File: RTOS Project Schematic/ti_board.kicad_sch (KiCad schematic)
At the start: 1 part, among them U2 TMS320LF2406

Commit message: Updated power rails
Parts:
- added JP1, JP2, JP3: Jumper_2_Open, symbol Jumper:Jumper_2_Open
- added JP6: Jumper_2_Bridged, symbol Jumper:Jumper_2_Bridged
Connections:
- net GND: now also U2.84 (GNDA), JP2.2 (B); no longer U2.19 (GND)
- net +3V3: now reaches U2.83 (VCCA)
- net +3V3: now also JP3.2 (B)
- net VCC: no longer names the net of U2.20 (VDD)
- new net +5V: JP1.2 (B), JP6.2 (B)
- new net AGND: JP2.1 (A)
- new net FTDI 3V3: JP3.1 (A)
- new net SWITCH: JP6.1 (A)
- new net USBVCC: JP1.1 (A)
- no-connect marks 0 -> 1
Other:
- note added: "3V3 - 5V REG"
- note added: "ONBOARD U12"
- note added: "USB"

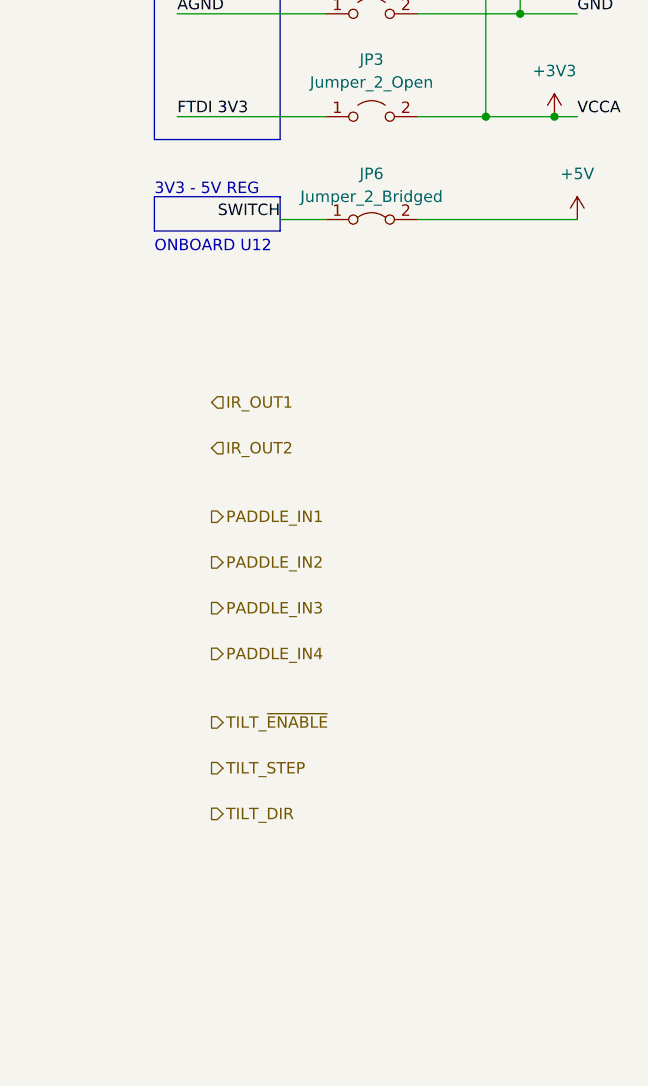
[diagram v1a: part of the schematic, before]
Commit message: Added preliminary microphone circuit
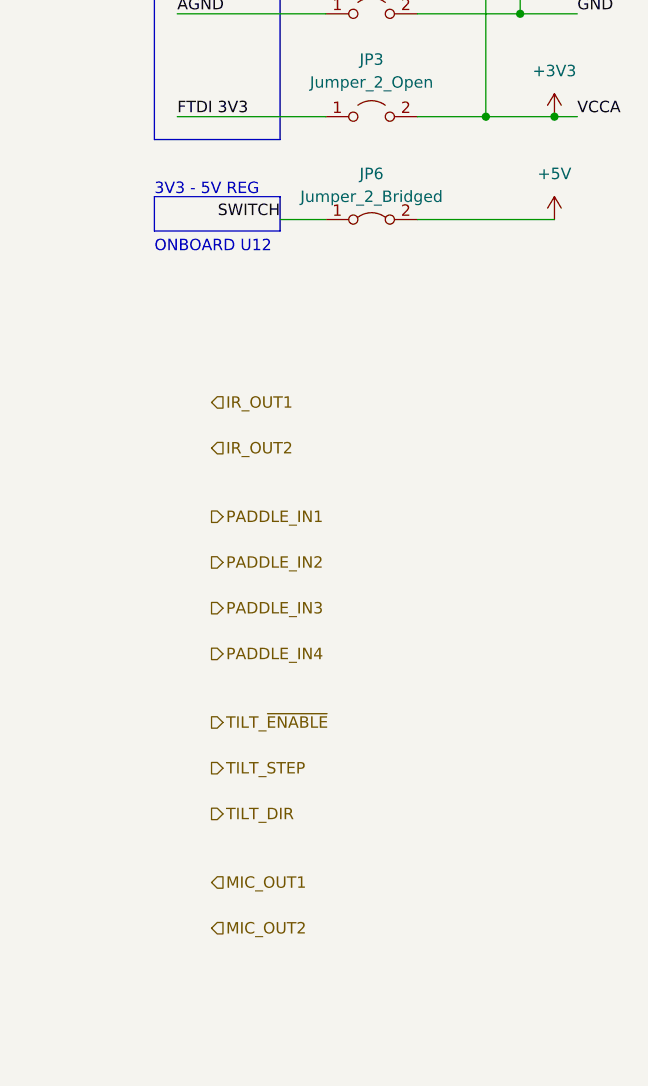
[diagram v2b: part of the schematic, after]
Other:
- company: (none) -> Eddie and Felix
- title: (none) -> TMS320C2837D
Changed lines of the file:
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@@
 (kicad_sch (version 20230121) (generator eeschema)
   (paper "A4")
+  (title_block
+    (title "TMS320C2837D")
+    (date "2023-11-29")
+    (rev "A")
+    (company "Eddie and Felix")
+  )
   (junction (at 233.68 39.37) (diameter 0) (color 0 0 0 0)
   )
@@
     (stroke (width 0) (type default))
   )
-  (wire (pts (xy 218.44 74.93) (xy 236.22 74.93))
+  (wire (pts (xy 218.44 74.93) (xy 233.68 74.93))
     (stroke (width 0) (type default))
   )
@@
     (effects (font (size 1.27 1.27)) (justify left bottom))
   )
+  (hierarchical_label "MIC_OUT2" (shape input) (at 195.58 153.67 0) (fields_autoplaced)
+    (effects (font (size 1.27 1.27)) (justify left))
+  )
   (hierarchical_label "IR_OUT2" (shape input) (at 195.58 100.33 0) (fields_autoplaced)
     (effects (font (size 1.27 1.27)) (justify left))
@@
   )
   (hierarchical_label "TILT_DIR" (shape output) (at 195.58 140.97 0) (fields_autoplaced)
+    (effects (font (size 1.27 1.27)) (justify left))
+  )
+  (hierarchical_label "MIC_OUT1" (shape input) (at 195.58 148.59 0) (fields_autoplaced)
     (effects (font (size 1.27 1.27)) (justify left))
   )
@@
     )
   )
-  (symbol (lib_id "power:+5V") (at 236.22 74.93 0) (unit 1)
+  (symbol (lib_id "power:+5V") (at 233.68 74.93 0) (unit 1)
     (in_bom yes) (on_board yes) (dnp no) (fields_autoplaced)
-    (property "Reference" "#PWR02" (at 236.22 78.74 0)
-      (effects (font (size 1.27 1.27)) hide)
-    )
-    (property "Value" "+5V" (at 236.22 69.85 0)
-      (effects (font (size 1.27 1.27)))
-    )
-    (property "Footprint" "" (at 236.22 74.93 0)
-      (effects (font (size 1.27 1.27)) hide)
-    )
-    (property "Datasheet" "" (at 236.22 74.93 0)
-      (effects (font (size 1.27 1.27)) hide)
-    )
+    (property "Reference" "#PWR02" (at 233.68 78.74 0)
+      (effects (font (size 1.27 1.27)) hide)
+    )
+    (property "Value" "+5V" (at 233.68 69.85 0)
+      (effects (font (size 1.27 1.27)))
+    )
+    (property "Footprint" "" (at 233.68 74.93 0)
+      (effects (font (size 1.27 1.27)) hide)
+    )
+    (property "Datasheet" "" (at 233.68 74.93 0)
+      (effects (font (size 1.27 1.27)) hide)
+    )

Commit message: Updated schematics
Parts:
- removed U2: TMS320LF2406, symbol MCU_Texas:TMS320LF2406
- added J1, J3: ConnA_01x10_Pin, symbol Connector:Conn_01x10_Pin
- added J2, J4: ConnB_01x10_Pin, symbol Connector:Conn_01x10_Pin
- added J5, J7: ConnC_01x10_Pin, symbol Connector:Conn_01x10_Pin
- added J6, J8: ConnD_01x10_Pin, symbol Connector:Conn_01x10_Pin
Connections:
- net MIC_OUT1: now also J3.6 (ADCINA3/ANALOGIN)
- net MIC_OUT2: now also J7.6 (ADCINA5/ANALOGIN)
- new net PI_SPI-CLK: J1.7 (GPIO60/SPICLKA)
- new net PI_SPI_CS: J2.9 (GPIO61/SPIACS)
- new net PI_SPI_MOSI: J2.5 (GPIO58/SPIAMOSI)
- new net PI_SPI_SIMO: J2.4 (GPIO59/SPIAMISO)
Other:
- moved on the sheet: JP1, JP2, JP3, JP6

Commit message: Updated schematic
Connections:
- net PI_SPI_SIMO renamed PI_SPI_MISO
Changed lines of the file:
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@@
     (effects (font (size 1.27 1.27)) (justify left))
   )
-  (hierarchical_label "PI_SPI_SIMO" (shape bidirectional) (at 250.19 39.37 0) (fields_autoplaced)
+  (hierarchical_label "PI_SPI_MISO" (shape bidirectional) (at 250.19 39.37 0) (fields_autoplaced)
     (effects (font (size 1.27 1.27)) (justify left))
   )
